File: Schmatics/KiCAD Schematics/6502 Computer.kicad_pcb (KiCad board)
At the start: 2 copper layers, 188.3 x 114.3 mm, 48 parts, among them J10 Conn_02x01, J11 RCJ-017, J12 Conn_02x03_Odd_Even, J2 Conn_02x20_Odd_Even, J3 Conn_01x04_Male, J4 Conn_02x03_Odd_Even, J5 Conn_02x08_Odd_Even, J6 Conn_01x06_Male, J7 Conn_02x03_Odd_Even, J8 Barrel_Jack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

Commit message: Scripts and Stuff
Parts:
- added C13: 10uf, Capacitor_THT:C_Radial_D5.0mm_H11.0mm_P2.00mm, F.Cu at (193.5, 121.5)
- added J13: Conn_02x01, Connector_PinHeader_2.54mm:PinHeader_2x01_P2.54mm_Vertical, F.Cu at (49.5, 75.0)
- added U9: LM7805_TO220, Package_TO_SOT_THT:TO-220-3_Vertical, F.Cu at (189.0, 111.4)
- C15: value 10uF -> 10uf; footprint Capacitor_SMD:CP_Elec_4x3.9 -> Capacitor_THT:C_Radial_D5.0mm_H11.0mm_P2.00mm
- moved C15 5.13 mm to (187.5, 121.5)
- moved R4 2.00 mm to (79.0, 125.0)
- moved R5 1.15 mm to (83.0, 125.0)
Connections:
- J2 pad 8: Net-(J2-Pin_8) -> Net-(J13-Pin_1)
- J5 pad 11: Net-(J12-Pin_2) -> Net-(J12-Pin_4)
- J5 pad 15: Net-(J12-Pin_1) -> Net-(J12-Pin_3)
- J8 pad 1: +5V -> Net-(U9-VI)
- R6 pad 1: +5V -> GND
- U1 pad 37: Net-(J2-Pin_8) -> Net-(J13-Pin_1)
- U3 pad 4: Net-(J12-Pin_4) -> Net-(J12-Pin_2)
- U3 pad 6: Net-(J12-Pin_3) -> Net-(J12-Pin_1)
- U4 pad 9: Net-(J2-Pin_8) -> Net-(J13-Pin_1)
- U5 pad 25: Net-(J2-Pin_8) -> Net-(J13-Pin_1)
- U5 pad 7: Net-(J12-Pin_2) -> Net-(J12-Pin_4)
- U5 pad 9: Net-(J12-Pin_1) -> Net-(J12-Pin_3)
- U7 pad 27: Net-(J2-Pin_8) -> Net-(J13-Pin_1)
- U7 pad 6: Net-(J2-Pin_8) -> Net-(J13-Pin_1)
- X1 pad 8: Net-(J2-Pin_8) -> Net-(J13-Pin_2)
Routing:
- net Net-(J13-Pin_1): track 0.00 -> 346.9 mm, vias 0 -> 2
- net Net-(J2-Pin_8): track 344.7 -> 0.00 mm, vias 4 -> 0
- net Net-(J12-Pin_2): track 219.4 -> 41.0 mm, vias 2 -> 0
- net Net-(J12-Pin_1): track 225.8 -> 49.3 mm, vias 2 -> 1
- net Net-(J12-Pin_4): track 38.4 -> 211.4 mm, vias 0 -> 3
- net Net-(J12-Pin_3): track 58.5 -> 204.9 mm, vias 4 -> 2
- net Net-(J2-Pin_20): track 222.0 -> 272.3 mm, vias 2 -> 5
- net Net-(J2-Pin_24): track 222.0 -> 263.2 mm
- net Net-(J2-Pin_34): track 294.2 -> 330.1 mm
- net GND: track 778.6 -> 814.1 mm, vias 6 -> 4
- net Net-(J2-Pin_30): track 228.7 -> 261.2 mm, vias 2 -> 3
- net Net-(J4-Pin_2): track 108.5 -> 76.3 mm
- net Net-(J2-Pin_14): track 252.1 -> 222.9 mm
- net Net-(U9-VI): track 0.00 -> 28.8 mm
- net Net-(J2-Pin_16): track 232.5 -> 260.3 mm, vias 3 -> 4
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
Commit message: MAJOR push with big basic improvements
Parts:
- added C16: 1uf, Capacitor_THT:C_Disc_D4.3mm_W1.9mm_P5.00mm, F.Cu at (70.1, 28.0)
- added C17: 1uf, Capacitor_THT:C_Disc_D4.3mm_W1.9mm_P5.00mm, F.Cu at (73.5, 28.0)
- added C18: 1uf, Capacitor_THT:C_Disc_D4.3mm_W1.9mm_P5.00mm, F.Cu at (77.0, 28.0)
- added C19: 1uf, Capacitor_THT:C_Disc_D4.3mm_W1.9mm_P5.00mm, F.Cu at (80.5, 28.0)
- added J1: DE9_Pins, Connector_Dsub:DSUB-9_Socket_Horizontal_P2.77x2.54mm_EdgePinOffset9.40mm, F.Cu at (38.1, 45.5)
- added J14: Conn_02x01, Connector_PinHeader_2.54mm:PinHeader_2x01_P2.54mm_Vertical, F.Cu at (201.0, 25.0)
- added J15: Conn_02x01, Connector_PinHeader_2.54mm:PinHeader_2x01_P2.54mm_Vertical, F.Cu at (201.0, 19.5)
- added J16: Conn_02x01, Connector_PinHeader_2.54mm:PinHeader_2x01_P2.54mm_Vertical, F.Cu at (119.0, 97.0)
- added R7: 10k, Resistor_THT:R_Axial_DIN0204_L3.6mm_D1.6mm_P7.62mm_Horizontal, F.Cu at (44.2, 57.4)
- added R8: 10k, Resistor_THT:R_Axial_DIN0204_L3.6mm_D1.6mm_P7.62mm_Horizontal, F.Cu at (44.2, 61.5)
- added R9: 10k, Resistor_THT:R_Axial_DIN0204_L3.6mm_D1.6mm_P7.62mm_Horizontal, F.Cu at (44.2, 65.5)
- added U10: MAX232, Package_DIP:DIP-16_W7.62mm, F.Cu at (43.0, 31.4)
- J10: value Conn_02x01 -> Conn_01x01; footprint Connector_PinHeader_2.54mm:PinHeader_2x01_P2.54mm_Vertical -> Connector_PinHeader_2.00mm:PinHeader_1x01_P2.00mm_Vertical
- J6: value Conn_01x06_Male -> Conn_01x03; footprint Connector_PinHeader_2.54mm:PinHeader_1x06_P2.54mm_Horizontal -> Connector_PinHeader_2.00mm:PinHeader_1x03_P2.00mm_Vertical
- SW1: footprint Button_Switch_THT:SW_PUSH_6mm_H5mm -> Button_Switch_THT:SW_PUSH_1P1T_6x3.5mm_H4.3_APEM_MJTP1243
- moved J6 188.0 mm to (216.5, 20.0), turned to 0 degrees
- moved J10 97.3 mm to (119.0, 94.0), turned to 180 degrees
- moved R1 65.6 mm to (104.0, 18.7), turned to -90 degrees
- moved RV1 61.9 mm to (163.0, 51.5), turned to 0 degrees
- moved SW1 57.4 mm to (93.0, 22.5), turned to 0 degrees
- moved C12 18.0 mm to (49.0, 93.5), turned to 90 degrees
- moved J8 11.5 mm to (210.5, 118.5)
- moved U3 11.4 mm to (130.5, 64.1)
- moved J7 11.4 mm to (184.0, 22.7)
- moved J5 11.3 mm to (215.0, 86.0)
- moved J2 11.1 mm to (215.0, 31.6)
- moved C13 9.96 mm to (203.0, 124.5)
- moved U9 9.02 mm to (197.9, 112.5)
- moved U5 8.64 mm to (62.4, 73.1)
- moved J3 8.54 mm to (168.3, 20.2)
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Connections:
- J6 pad 1: unconnected-(J6-Pin_1-Pad1) -> Net-(J14-Pin_1)
- J6 pad 2: GND -> Net-(J2-Pin_7)
- J6 pad 3: Net-(J4-Pin_5) -> Net-(J15-Pin_1)
- J7 pad 1: +5V -> Net-(J7-Pin_1)
- J7 pad 3: +5V -> Net-(J7-Pin_3)
- J7 pad 5: +5V -> Net-(J7-Pin_5)
- U5 pad 21: Net-(J2-Pin_7) -> Net-(J15-Pin_1)
- U7 pad 26: Net-(J10-Pin_1) -> Net-(J14-Pin_1)
- U7 pad 6: Net-(J13-Pin_1) -> Net-(J16-Pin_1)
- U7 pad 7: unconnected-(U7-XLT0-Pad7) -> Net-(J10-Pin_1)
- U7 pad 8: unconnected-(U7-~{RTS}-Pad8) -> Net-(U10-T2IN)
- UA1 pad 1: +5V -> Net-(J2-Pin_2)
- UA1 pad 26: Net-(J6-Pin_5) -> Net-(U10-T2IN)
- UB1 pad 1: +5V -> Net-(J2-Pin_2)
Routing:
- net Net-(J14-Pin_1): track 0.00 -> 194.8 mm, vias 0 -> 2
- net Net-(J7-Pin_3): track 0.00 -> 188.7 mm, vias 0 -> 1
- net Net-(J7-Pin_5): track 0.00 -> 184.2 mm, vias 0 -> 1
- net Net-(J7-Pin_1): track 0.00 -> 179.0 mm, vias 0 -> 1
- net Net-(J6-Pin_5): track 171.9 -> 0.00 mm, vias 2 -> 0
- net Net-(U10-T2IN): track 0.00 -> 147.1 mm, vias 0 -> 2
- net Net-(J15-Pin_1): track 0.00 -> 143.5 mm, vias 0 -> 3
- net Net-(J10-Pin_1): track 159.3 -> 39.1 mm, vias 2 -> 1
- net +5V: track 689.5 -> 781.9 mm, vias 5 -> 1
- net Net-(J2-Pin_2): track 275.2 -> 361.7 mm, vias 2 -> 4
- net GND: track 814.1 -> 896.2 mm, vias 4 -> 1
- net Net-(U10-C2-): track 0.00 -> 47.8 mm, vias 0 -> 1
- net Net-(U10-VS-): track 0.00 -> 45.0 mm
- net Net-(U10-C2+): track 0.00 -> 39.4 mm
- net Net-(U10-VS+): track 0.00 -> 39.1 mm
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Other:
- board size 188.3 x 114.3 mm -> 199.6 x 114.2 mm
- board text added: "$8000 R MS-BASIC"
- board text added: "~{IRQ (6522})"
- board text removed: "CTS(NC)"
- board text removed: "GND"
- board text removed: "RESET"
- board text removed: "RTS"
- board text removed: "VCC(NC)"

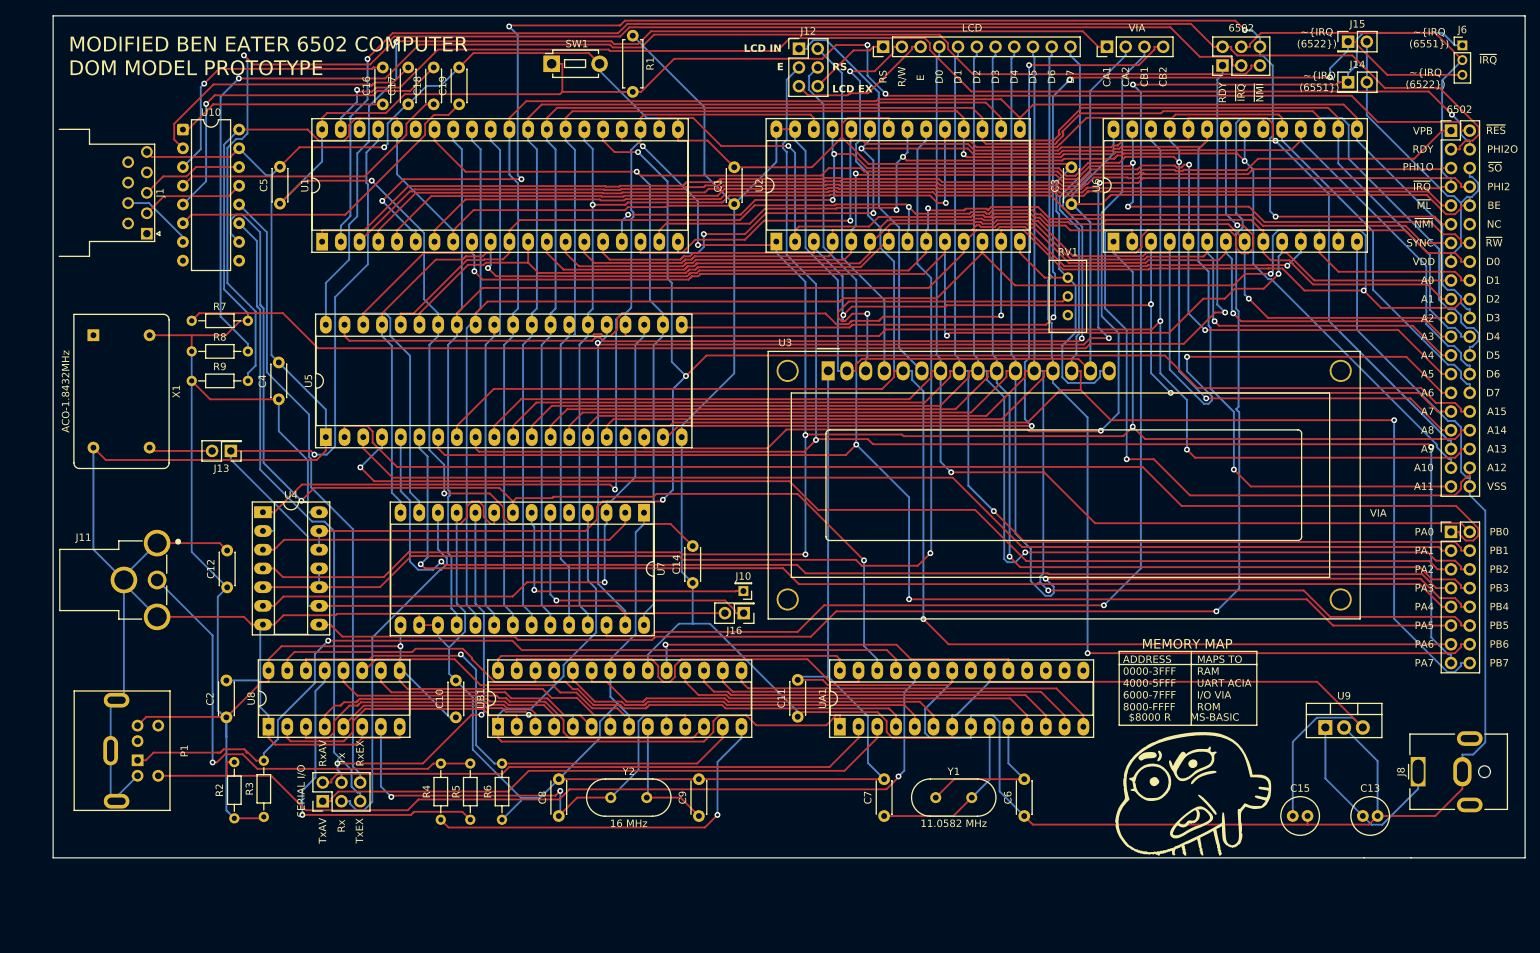
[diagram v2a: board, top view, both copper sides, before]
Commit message: Schumatic Sound Chip
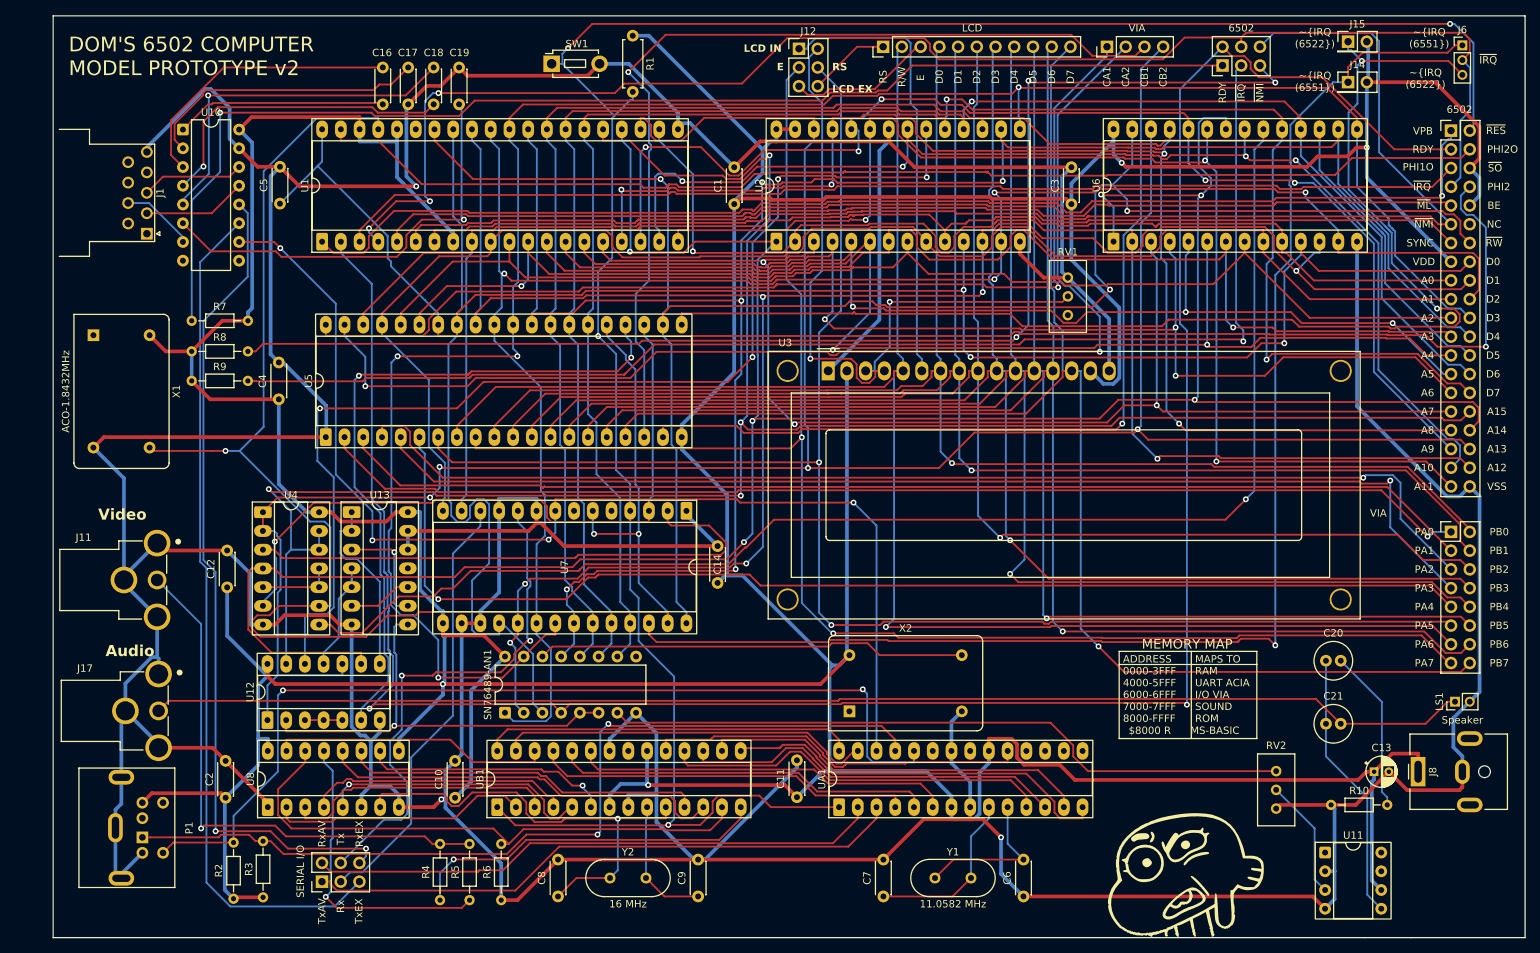
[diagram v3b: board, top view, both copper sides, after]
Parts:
- removed C15: 10uf, Capacitor_THT:C_Radial_D5.0mm_H11.0mm_P2.00mm
- removed J10: Conn_01x01, Connector_PinHeader_2.00mm:PinHeader_1x01_P2.00mm_Vertical
- removed J13, J16: Conn_02x01, Connector_PinHeader_2.54mm:PinHeader_2x01_P2.54mm_Vertical
- removed U9: LM7805_TO220, Package_TO_SOT_THT:TO-220-3_Vertical
- added C20: 0.05uF, Capacitor_THT:C_Radial_D5.0mm_H11.0mm_P2.00mm, F.Cu at (198.0, 103.5)
- added C21: 20uF, Capacitor_THT:C_Radial_D5.0mm_H11.0mm_P2.00mm, F.Cu at (198.0, 112.0)
- added J17: RCJ-017, Connector_RCA:CUI_RCJ-017, F.Cu at (33.8, 110.2)
- added LS1: Speaker, Connector_PinHeader_2.00mm:PinHeader_1x02_P2.00mm_Vertical, F.Cu at (215.5, 109.0)
- added R10: 10 Ohm, Resistor_THT:R_Axial_DIN0204_L3.6mm_D1.6mm_P7.62mm_Horizontal, F.Cu at (198.7, 123.0)
- added RV2: R_POT_TRIM_US, Potentiometer_THT:Potentiometer_Bourns_3386C_Horizontal, F.Cu at (191.2, 118.4)
- added SN76489-AN1: ~, Package_DIP:DIP-16_W7.62mm, F.Cu at (86.7, 110.5)
- added U11: LM386, Package_DIP:DIP-8_W7.62mm_Socket, F.Cu at (197.9, 129.5)
- added U12: 74HC00, Package_DIP:DIP-14_W7.62mm_Socket_LongPads, F.Cu at (54.5, 111.5)
- added U13: 74HC00, Package_DIP:DIP-14_W7.62mm_Socket_LongPads, F.Cu at (65.9, 83.3)
- added X2: 4MHz, Oscillator:Oscillator_DIP-14, F.Cu at (133.4, 110.3)
- C13: footprint Capacitor_THT:C_Radial_D5.0mm_H11.0mm_P2.00mm -> Capacitor_THT:CP_Radial_D4.0mm_P2.00mm
- moved G*** 11.0 mm to (178.3, 128.9)
- moved C6 10.9 mm to (157.0, 135.4)
- moved C7 10.9 mm to (138.0, 135.4)
- moved C8 10.9 mm to (93.9, 135.4)
- moved C9 10.9 mm to (112.9, 135.4)
- moved R2 10.9 mm to (49.9, 135.7)
- moved R4 10.9 mm to (77.9, 135.9)
- moved R5 10.9 mm to (81.9, 135.9)
- moved R6 10.9 mm to (86.2, 135.9)
- moved Y1 10.9 mm to (145.0, 132.9)
- moved Y2 10.9 mm to (100.9, 132.9)
- moved C10 10.9 mm to (79.9, 122.0)
- moved C11 10.9 mm to (126.3, 122.0)
- moved C2 10.9 mm to (48.8, 122.0)
- moved J4 10.9 mm to (61.9, 133.4)
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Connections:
- C13 pad 1: Net-(U9-VI) -> +5V
- J2 pad 8: Net-(J13-Pin_1) -> Net-(J2-Pin_8)
- J8 pad 1: Net-(U9-VI) -> +5V
- U1 pad 37: Net-(J13-Pin_1) -> Net-(J2-Pin_8)
- U4 pad 9: Net-(J13-Pin_1) -> Net-(J2-Pin_8)
- U5 pad 24: Net-(J2-Pin_36) -> Net-(U5-CS1)
- U5 pad 25: Net-(J13-Pin_1) -> Net-(J2-Pin_8)
- U7 pad 27: Net-(J13-Pin_1) -> Net-(J2-Pin_8)
- U7 pad 6: Net-(J16-Pin_1) -> Net-(J2-Pin_8)
- U7 pad 7: Net-(J10-Pin_1) -> unconnected-(U7-XLT0-Pad7)
- X1 pad 8: Net-(J13-Pin_2) -> Net-(J2-Pin_8)
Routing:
- net Net-(J2-Pin_8): track 0.00 -> 370.4 mm, vias 0 -> 4
- net Net-(J13-Pin_1): track 329.9 -> 0.00 mm, vias 4 -> 0
- net Net-(J17-V_In): track 0.00 -> 179.4 mm
- net Net-(J2-Pin_3): track 190.8 -> 310.3 mm, vias 1 -> 2
- net +5V: track 781.9 -> 879.9 mm, vias 1 -> 4
- net Net-(SN76489-AN1-A_Out): track 0.00 -> 93.5 mm
- net Net-(U5-CS1): track 0.00 -> 93.4 mm, vias 0 -> 2
- net Net-(SN76489-AN1-CE_): track 0.00 -> 60.6 mm, vias 0 -> 1
- net Net-(SN76489-AN1-CLK): track 0.00 -> 58.5 mm
- net Net-(J2-Pin_18): track 223.9 -> 275.8 mm, vias 1 -> 6
- net GND: track 896.2 -> 948.1 mm, vias 1 -> 3
- net Net-(J2-Pin_32): track 220.7 -> 272.4 mm, vias 3 -> 4
- net Net-(J2-Pin_22): track 224.8 -> 276.3 mm, vias 0 -> 4
- net Net-(J2-Pin_16): track 221.8 -> 271.7 mm, vias 1 -> 3
- net Net-(J2-Pin_24): track 226.3 -> 273.0 mm, vias 0 -> 5
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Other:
- board size 199.6 x 114.2 mm -> 199.6 x 125 mm
- board text added: "ADDRESS 0000-3FFF 4000-5FFF 6000-6FFF 7000-7FFF 8000-FFFF"
- board text added: "Audio"
- board text added: "DOM'S 6502 COMPUTER MODEL PROTOTYPE v2"
- board text added: "MAPS TO RAM UART ACIA I/O VIA SOUND ROM"
- board text added: "Video"
- board text removed: "ADDRESS 0000-3FFF 4000-5FFF 6000-7FFF 8000-FFFF"
- board text removed: "MAPS TO RAM UART ACIA I/O VIA ROM"
- board text removed: "MODIFIED BEN EATER 6502 COMPUTER DOM MODEL PROTOTYPE"
